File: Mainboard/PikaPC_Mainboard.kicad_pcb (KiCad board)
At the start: 2 copper layers, 190.5 x 147.3 mm, 80 parts, among them J1 Conn_02x05_Odd_Even, J10 Conn_01x08, J11 Conn_01x08, J12 Conn_01x08, J13 Conn_01x08, J14 Conn_01x08, J15 Conn_01x08, J16 Conn_01x08, J17 Conn_01x08, J18 Conn_01x10, J19 Conn_02x05_Odd_Even, J5 DIN41612_03x32_C_Split, J6 Mini-DIN-6, J7 Mini-DIN-6, J8 Conn_01x06, J9 Conn_01x08, SW1 SW_Push_DPDT, SW2 SW_Push, U1 PPC403GA, U10 74LS07, U11 86C325, U12 GD75232N, U13 74LVC125, U14 MCP120-315GI/TO, U15 AS6C4008-55PCN, U16 AS6C4008-55PCN, U17 ATF1504, U18 T224162B, U19 T224162B, U2 SN74LVC245A, U20 T224162B, U21 T224162B, U3 SST39VF010, U4 SN74LVC245A, U5 SN74LVC245A, U6 SN74LVC245A, U7 8042 PS/2, U8 ATF22V10C, U9 74LS04, Y1 25M, Y2 7M3728, Y3 14M31818

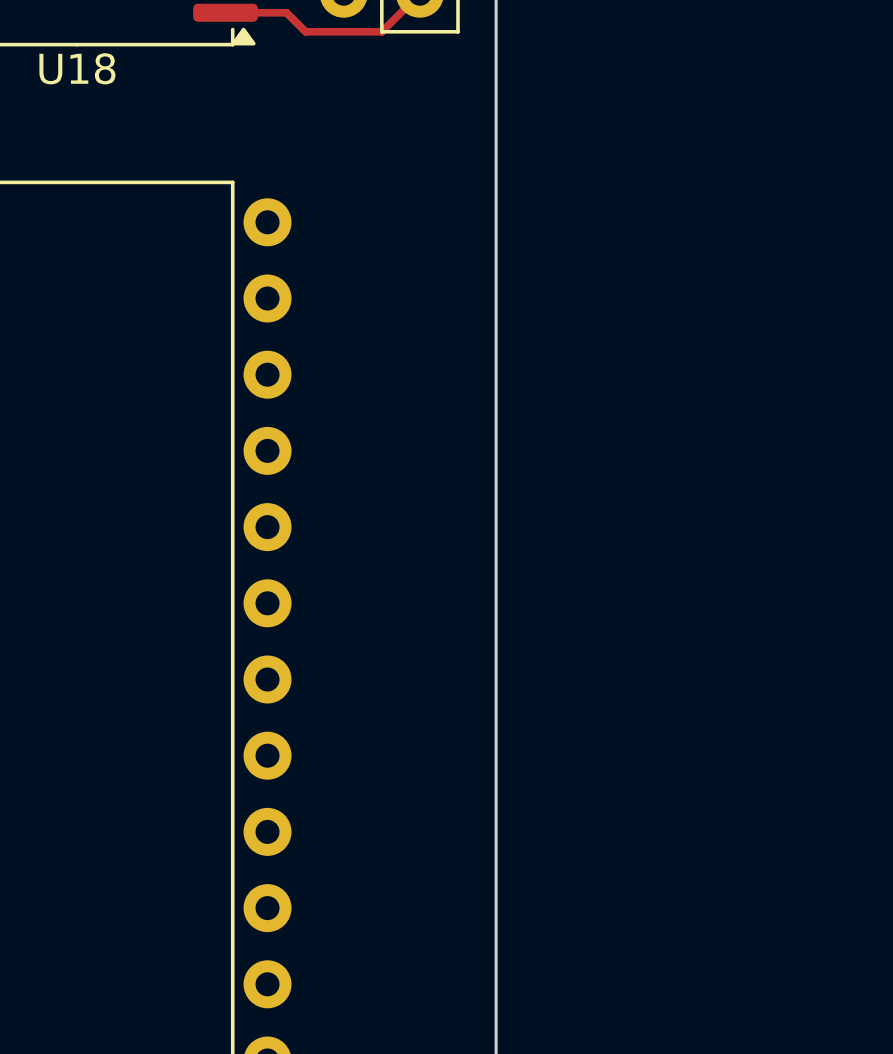
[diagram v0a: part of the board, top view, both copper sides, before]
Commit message: ViRGE Strapping pulldowns should be on VMD not PD
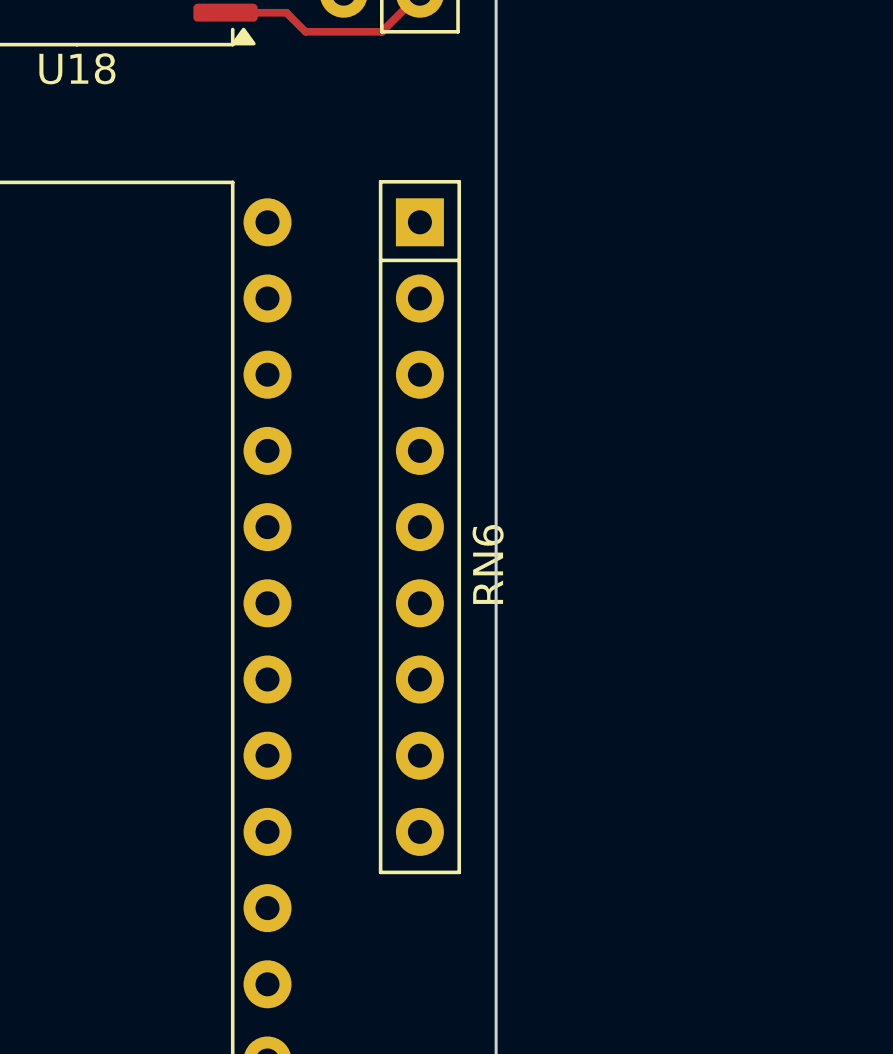
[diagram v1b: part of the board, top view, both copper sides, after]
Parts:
- added RN6: 9A103J, Resistor_THT:R_Array_SIP9, F.Cu at (259.1, 101.6)
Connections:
- RN5 pad 2: /PD1 -> unconnected-(RN5-R1-Pad2)
- RN5 pad 3: /PD2 -> unconnected-(RN5-R2-Pad3)
- RN5 pad 4: /PD4 -> unconnected-(RN5-R3-Pad4)
- RN5 pad 5: /PD5 -> unconnected-(RN5-R4-Pad5)
- RN5 pad 6: /PD6 -> unconnected-(RN5-R5-Pad6)

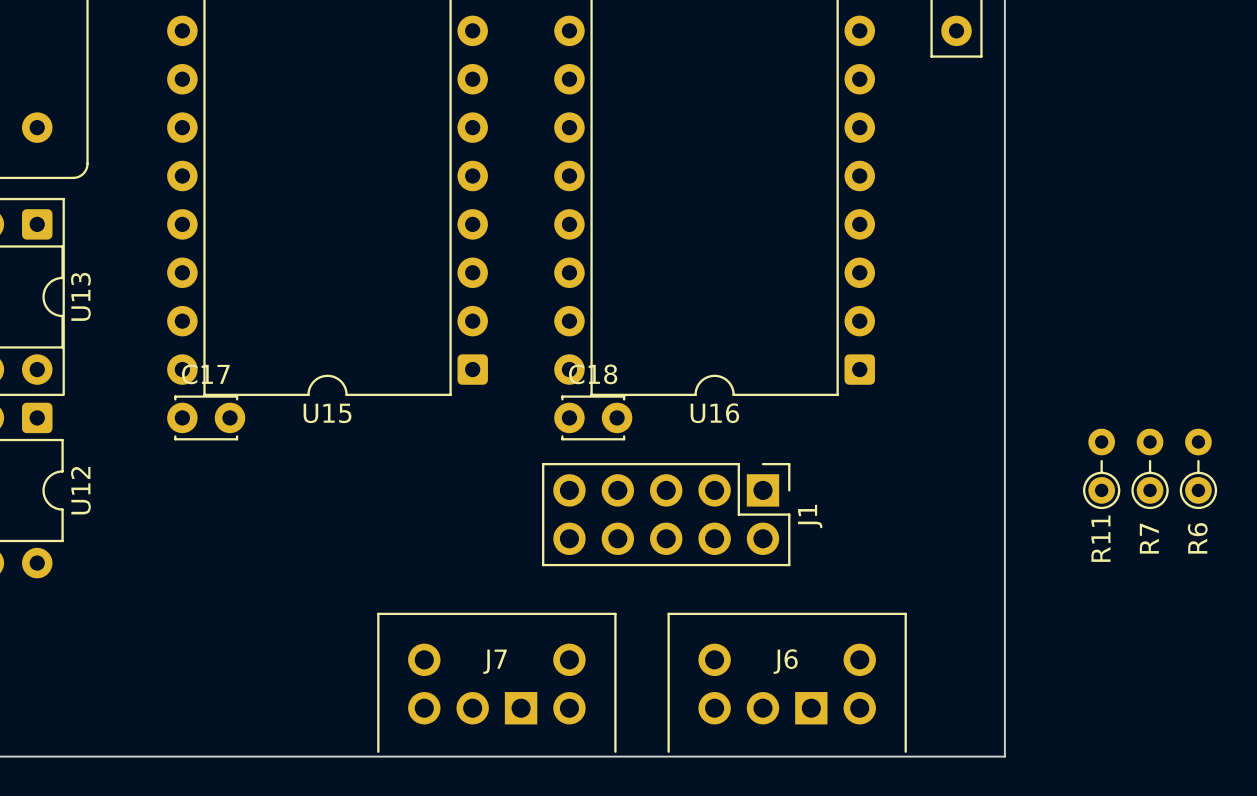
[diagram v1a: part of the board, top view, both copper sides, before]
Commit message: VGA output use full-size header, add ferrite beads
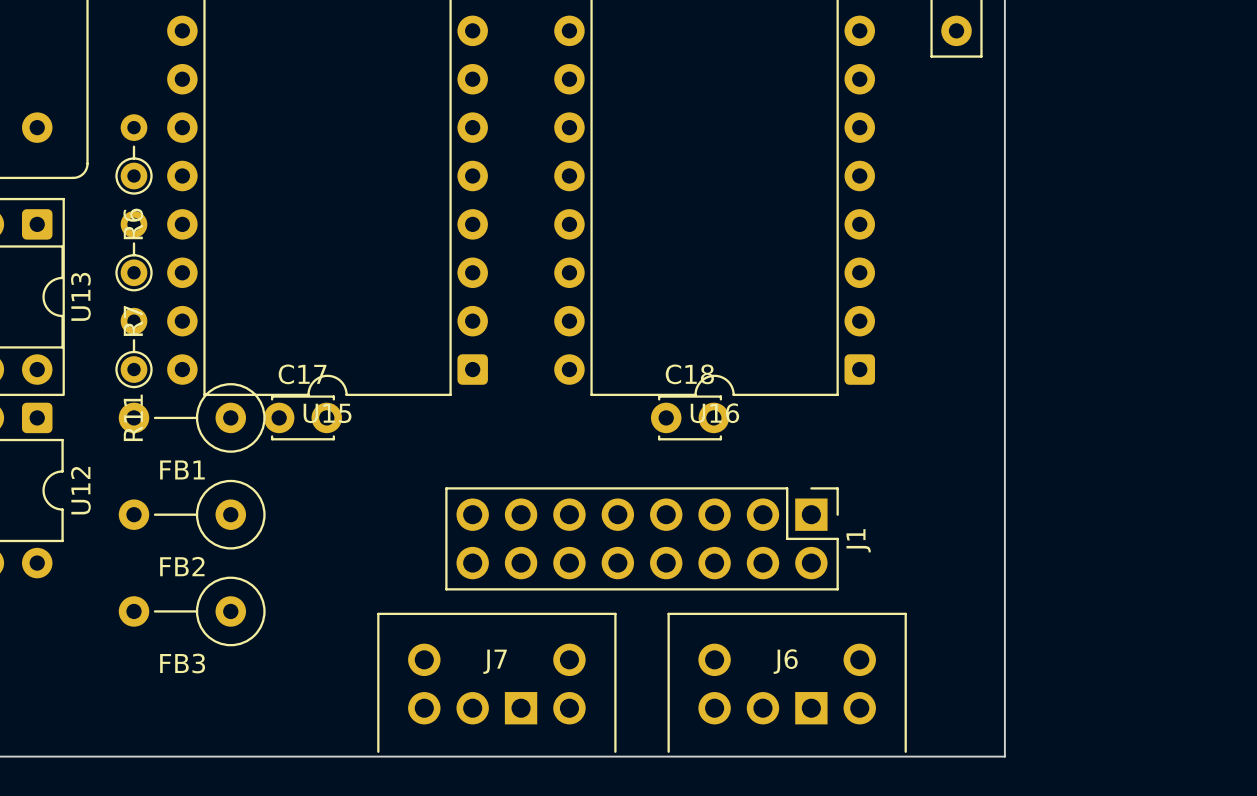
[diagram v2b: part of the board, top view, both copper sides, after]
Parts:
- added FB1: FerriteBead, Inductor_THT:L_Axial_L7.0mm_D3.3mm_P5.08mm_Vertical_Fastron_MICC, F.Cu at (221.0, 142.2)
- added FB2: FerriteBead, Inductor_THT:L_Axial_L7.0mm_D3.3mm_P5.08mm_Vertical_Fastron_MICC, F.Cu at (221.0, 147.3)
- added FB3: FerriteBead, Inductor_THT:L_Axial_L7.0mm_D3.3mm_P5.08mm_Vertical_Fastron_MICC, F.Cu at (221.0, 152.4)
- J1: value Conn_02x05_Odd_Even -> Conn_02x08_Odd_Even; footprint Connector_PinHeader_2.54mm:PinHeader_2x05_P2.54mm_Vertical -> Connector_PinHeader_2.54mm:PinHeader_2x08_P2.54mm_Vertical
- moved R6 58.3 mm to (215.9, 129.5)
- moved R7 54.5 mm to (215.9, 134.6)
- moved R11 51.2 mm to (215.9, 139.7)
- moved C17 5.08 mm to (223.5, 142.2)
- moved C18 5.08 mm to (243.8, 142.2)
- moved J1 2.84 mm to (251.5, 147.3)
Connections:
- J1 pad 1: /Vid-R -> /Vid-R-Out
- J1 pad 2: GND -> /Vid-G-Out
- J1 pad 3: /Vid-G -> /Vid-B-Out
- J1 pad 4: GND -> unconnected-(J1-Pin_4-Pad4)
- J1 pad 5: /Vid-B -> GND
- J1 pad 7: /Vid-H -> GND
- J1 pad 9: /Vid-V -> unconnected-(J1-Pin_9-Pad9)

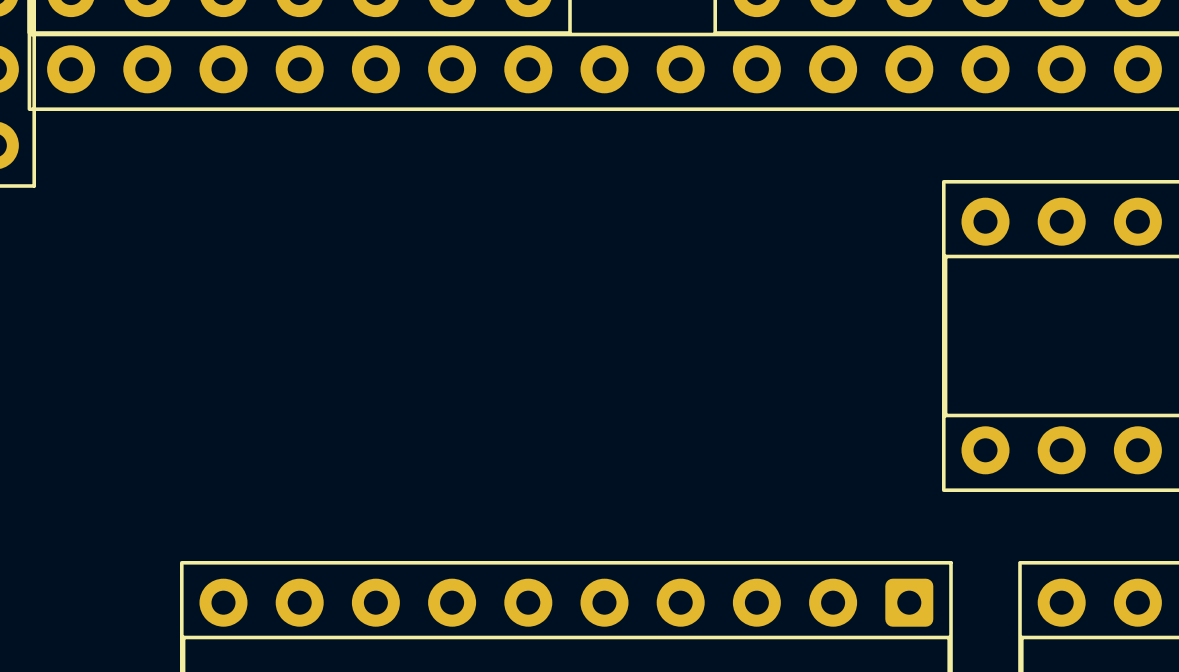
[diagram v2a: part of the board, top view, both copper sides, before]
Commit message: Troubleshooting ViRGE communication
- use A[25:23] for ViRGE SAUP[2:1] & M/IO# signals
- add pull-up resistors to ViRGE ready & loca signals
- adjust bank registers for new memory map
- add forth test program for VGA init & ID
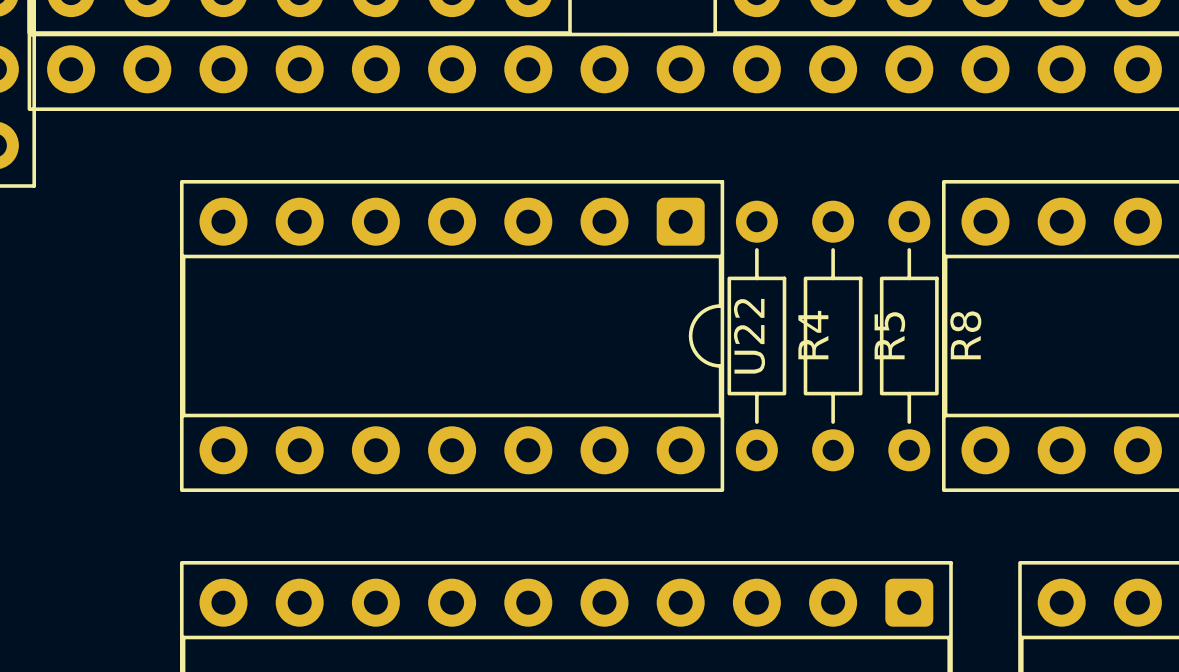
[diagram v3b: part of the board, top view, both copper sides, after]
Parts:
- added R4: 1k, Resistor_THT:R_Axial_DIN0204_L3.6mm_D1.6mm_P7.62mm_Horizontal, F.Cu at (99.1, 53.3)
- added R5: 1k, Resistor_THT:R_Axial_DIN0204_L3.6mm_D1.6mm_P7.62mm_Horizontal, F.Cu at (101.6, 53.3)
- added R8: 1k, Resistor_THT:R_Axial_DIN0204_L3.6mm_D1.6mm_P7.62mm_Horizontal, F.Cu at (104.1, 53.3)
- added U22: 74LVC125, Package_DIP:DIP-14_W7.62mm_Socket, F.Cu at (96.5, 53.3)
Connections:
- RN4 pad 7: unconnected-(RN4-R6-Pad7) -> /~{VID-RDYIN}
- RN4 pad 8: unconnected-(RN4-R7-Pad8) -> /~{VID-SRDYn}
- RN4 pad 9: unconnected-(RN4-R8-Pad9) -> /~{VID-LOCA}
- U11 pad 24: unconnected-(U11A-~{LOCA}-Pad24) -> /~{VID-LOCA}
- U11 pad 25: /~{CS3} -> /VID-SAUP1
- U11 pad 50: /~{CS2} -> /VID-SAUP2
- U11 pad 8: /~{CS3} -> /A23
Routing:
- net /~{CS3}: track 42.1 -> 17.8 mm
- net /VID-SAUP1: track 0.00 -> 13.7 mm
- net /~{CS2}: track 28.1 -> 15.0 mm
- net /VID-SAUP2: track 0.00 -> 13.1 mm
- net unconnected-(U11A-~{LOCA}-Pad24): track 11.0 -> 0.00 mm
- net /~{VID-LOCA}: track 0.00 -> 11.0 mm
- net /A23: track 16.0 -> 26.5 mm

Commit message: ViRGE byte select fixes
- swap data bus byte order
- decode low address bits for write byte selects
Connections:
- U8 pad 10: /A0/~{WBE3} -> /~{WBE0}
- U8 pad 7: /~{WBE0} -> /A0/~{WBE3}
- U8 pad 8: /~{WBE1} -> /A1/~{WBE2}
- U8 pad 9: /A1/~{WBE2} -> /~{WBE1}
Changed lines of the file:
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@@
 			(layers "*.Cu" "*.Mask")
 			(remove_unused_layers no)
-			(net 121 "/~{WBE0}")
+			(net 163 "/A0{slash}~{WBE3}")
 			(pinfunction "I7")
 			(pintype "input")
@@
 			(layers "*.Cu" "*.Mask")
 			(remove_unused_layers no)
-			(net 122 "/~{WBE1}")
+			(net 164 "/A1{slash}~{WBE2}")
 			(pinfunction "I8")
 			(pintype "input")
@@
 			(layers "*.Cu" "*.Mask")
 			(remove_unused_layers no)
-			(net 164 "/A1{slash}~{WBE2}")
+			(net 122 "/~{WBE1}")
 			(pinfunction "I9")
 			(pintype "input")
@@
 			(layers "*.Cu" "*.Mask")
 			(remove_unused_layers no)
-			(net 163 "/A0{slash}~{WBE3}")
+			(net 121 "/~{WBE0}")
 			(pinfunction "I10")
 			(pintype "input")

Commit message: ViRGE byte select fixes 2
- swap byte select output order on bus control logic
- update VGA initialization forth program
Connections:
- net /A0/~{WBE3} renamed /A0/~{WBE0}
- net /A1/~{WBE2} renamed /A1/~{WBE1}
- net /~{WBE0} renamed /~{WBE3}
- net /~{WBE1} renamed /~{WBE2}
- U11 pad 1: /PD29 -> /PD5
- U11 pad 10: /PD23 -> /PD15
- U11 pad 11: /PD22 -> /PD14
- U11 pad 13: /PD21 -> /PD13
- U11 pad 14: /PD20 -> /PD12
- U11 pad 15: /PD19 -> /PD11
- U11 pad 16: /PD18 -> /PD10
- U11 pad 17: /PD17 -> /PD9
- U11 pad 18: /PD16 -> /PD8
- U11 pad 2: /PD28 -> /PD4
- U11 pad 207: /PD31 -> /PD7
- U11 pad 208: /PD30 -> /PD6
- U11 pad 28: /PD15 -> /PD23
- U11 pad 29: /PD14 -> /PD22
- U11 pad 3: /PD27 -> /PD3
- U11 pad 30: /PD13 -> /PD21
- U11 pad 31: /PD12 -> /PD20
- U11 pad 33: /PD11 -> /PD19
- U11 pad 34: /PD10 -> /PD18
- U11 pad 35: /PD9 -> /PD17
- U11 pad 36: /PD8 -> /PD16
- U11 pad 39: /PD7 -> /PD31
- U11 pad 4: /PD26 -> /PD2
- U11 pad 40: /PD6 -> /PD30
- U11 pad 41: /PD5 -> /PD29
- U11 pad 42: /PD4 -> /PD28
- U11 pad 43: /PD3 -> /PD27
- U11 pad 44: /PD2 -> /PD26
- U11 pad 45: /PD1 -> /PD25
- U11 pad 46: /PD0 -> /PD24
- U11 pad 5: /PD25 -> /PD1
- U11 pad 6: /PD24 -> /PD0
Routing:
- net GND: track 610.0 -> 645.7 mm
- net /~{WBE3}: track 19.8 -> 0.00 mm
- net /~{WBE2}: track 15.8 -> 0.00 mm
- net /PD26: track 18.4 -> 10.6 mm
- net /PD2: track 10.6 -> 18.4 mm
- net /PD5: track 10.2 -> 15.1 mm
- net /PD29: track 15.1 -> 10.2 mm
- net /PD20: track 9.67 -> 14.3 mm
- net /PD12: track 14.3 -> 9.67 mm
- net /PD7: track 13.0 -> 17.0 mm
- net /PD31: track 17.0 -> 13.0 mm
- net /PD6: track 15.5 -> 19.6 mm
- net /PD30: track 19.6 -> 15.5 mm
- net /PD21: track 15.4 -> 11.7 mm
- net /PD13: track 11.7 -> 15.4 mm
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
